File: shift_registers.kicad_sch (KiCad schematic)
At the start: 8 parts, among them U701 74HC595, U702 74HC595, U703 74HC595, U704 74HC595

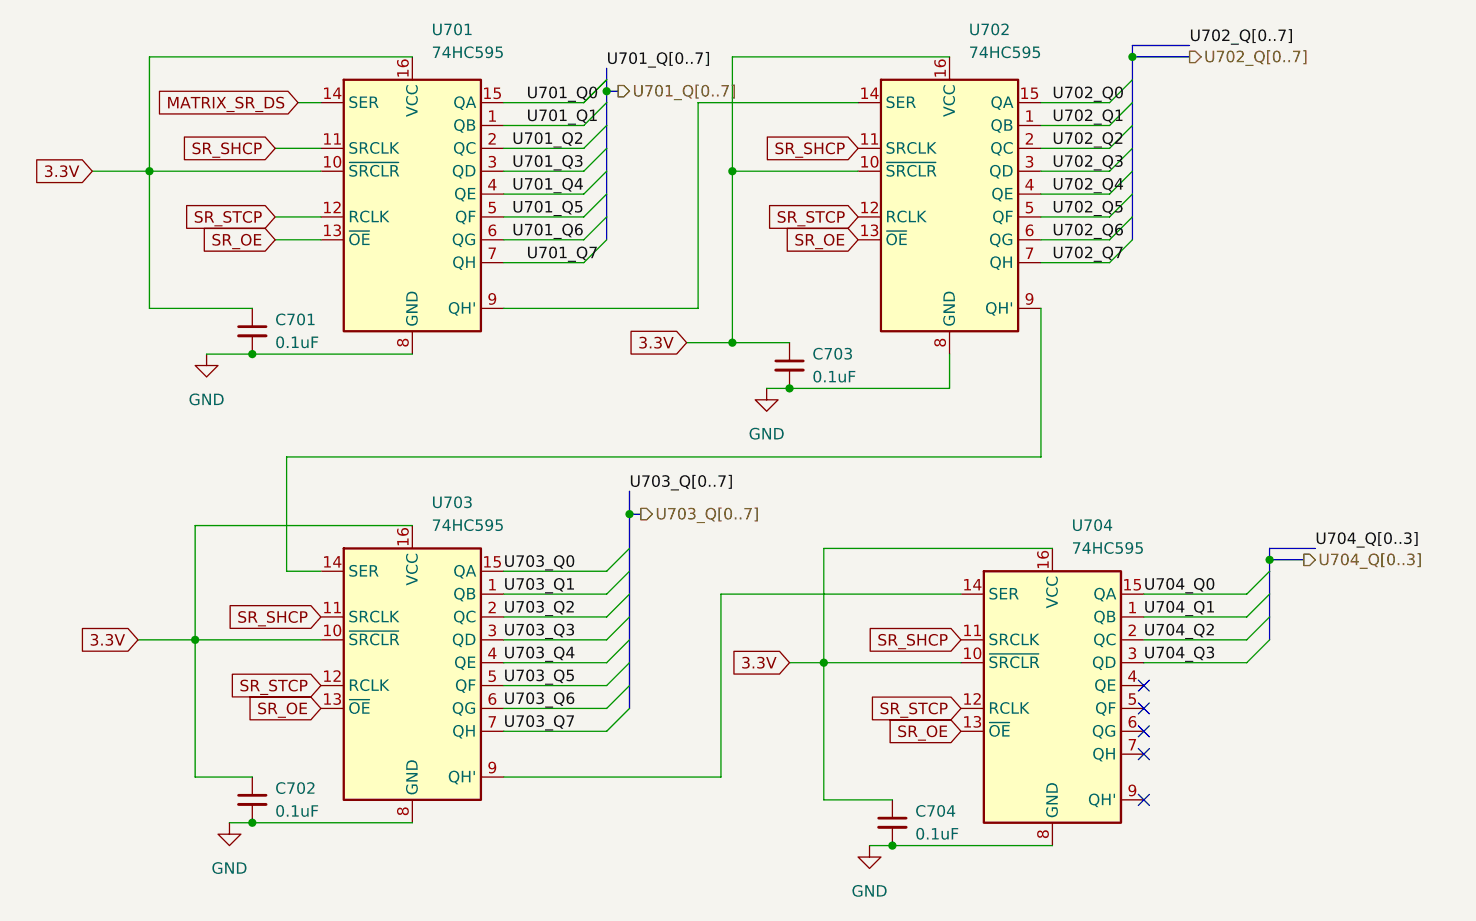
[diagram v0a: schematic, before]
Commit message: Removed LED Shift registers and replaced them with PCA9685 PWM controllers, Also changed LEDs to RGB LEDs.
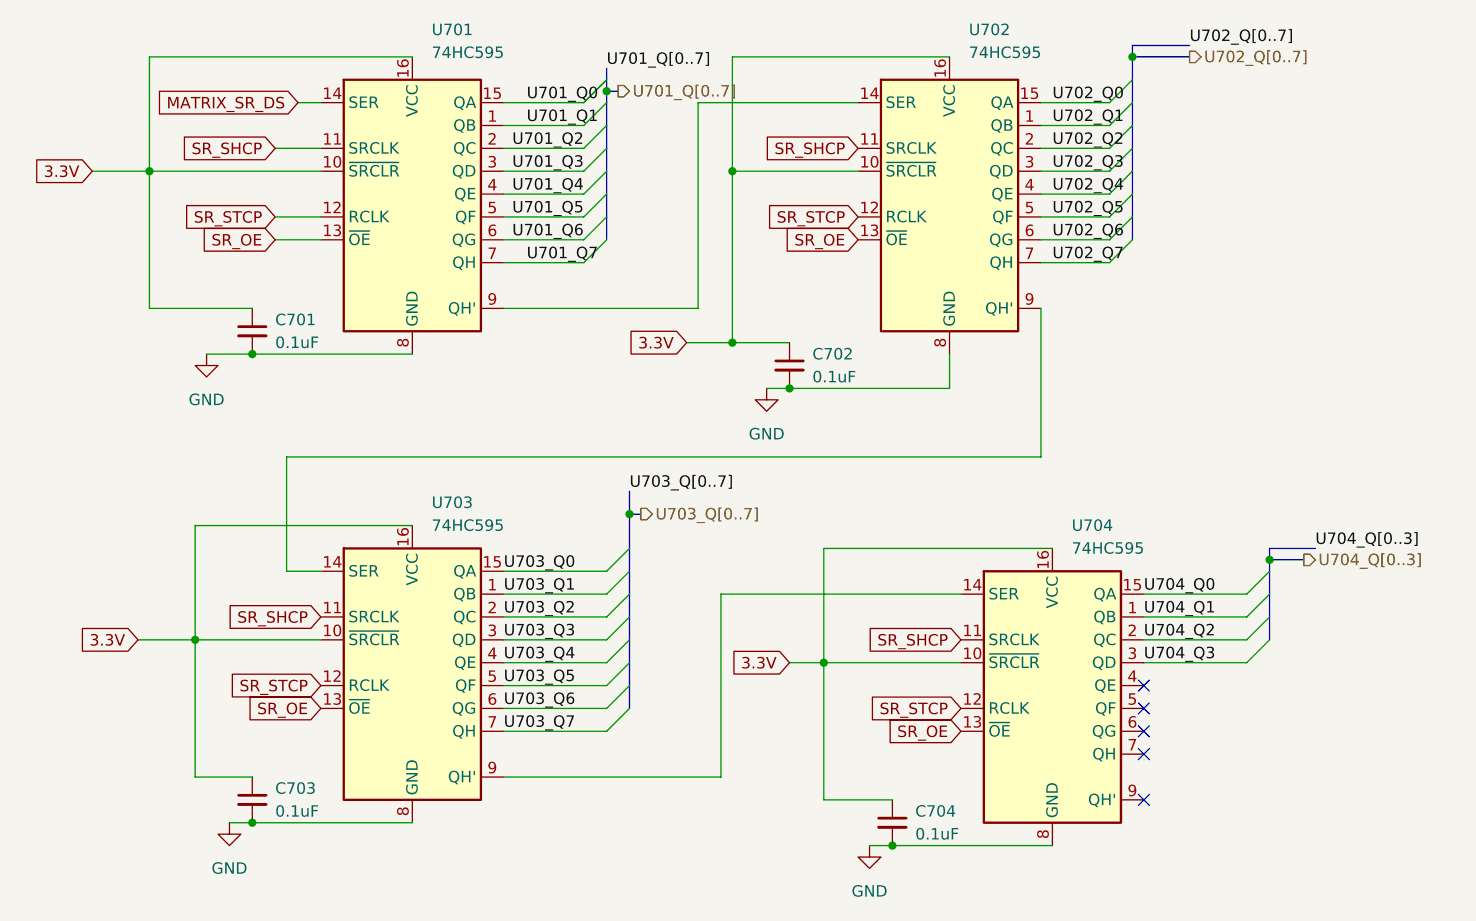
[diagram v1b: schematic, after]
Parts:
- renumbered C703 to C702, C702 to C703
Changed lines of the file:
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@@
 		(dnp no)
 		(fields_autoplaced yes)
-		(property "Reference" "C702"
+		(property "Reference" "C703"
 			(at 55.88 110.4962 0)
 			(effects
@@
 			(project "circuit"
 				(path "/420e3d7a-6c9a-4806-b4be-05d56aeb21de/4760116a-7aa4-465f-87dd-a53dbe30c185"
-					(reference "C702")
+					(reference "C703")
 					(unit 1)
 				)
@@
 		(dnp no)
 		(fields_autoplaced yes)
-		(property "Reference" "#PWR0702"
+		(property "Reference" "#PWR0703"
 			(at 50.8 120.65 0)
 			(effects
@@
 			(project "circuit"
 				(path "/420e3d7a-6c9a-4806-b4be-05d56aeb21de/4760116a-7aa4-465f-87dd-a53dbe30c185"
-					(reference "#PWR0702")
+					(reference "#PWR0703")
 					(unit 1)
 				)
@@
 		(dnp no)
 		(fields_autoplaced yes)
-		(property "Reference" "#PWR0703"
+		(property "Reference" "#PWR0702"
 			(at 110.49 72.39 0)
 			(effects
@@
 			(project "circuit"
 				(path "/420e3d7a-6c9a-4806-b4be-05d56aeb21de/4760116a-7aa4-465f-87dd-a53dbe30c185"
-					(reference "#PWR0703")
+					(reference "#PWR0702")
 					(unit 1)
 				)
@@
 		(dnp no)
 		(fields_autoplaced yes)
-		(property "Reference" "C703"
+		(property "Reference" "C702"
 			(at 115.57 62.2362 0)
 			(effects
@@
 			(project "circuit"
 				(path "/420e3d7a-6c9a-4806-b4be-05d56aeb21de/4760116a-7aa4-465f-87dd-a53dbe30c185"
-					(reference "C703")
-					(unit 1)
-				)
+					(reference "C702")
+					(unit 1)
+				)
